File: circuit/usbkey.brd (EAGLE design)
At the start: 78.4 x 68.6 mm, 29 parts, among them IC1 ATmega168P, Q1 16MHz, X2 USB

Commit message: update
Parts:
- removed C5: 1u, resistor:C025-024X044
- removed C6: 0.1u, resistor:C025-024X044
- removed JP1: AVR-ISP-6VERT, avr-7:AVR-ISP-6
- removed JP3: (no value), pinhead:1X09
- removed LED, OUTPUT, SPEAKER: (no value), pinhead:1X02
- removed R5: VARISTOR, varistor:R-5
- removed R9: 1k, resistor:0204/7
- added D3, D4: 5V, diode:DO35Z10
- added P1: SPEAKER, pinhead:1X02
- added P2: LED, pinhead:1X02
- added P3: OUTPUT, pinhead:1X02
- added PISP: AVR-ISP-6VERT, avr-7:AVR-ISP-6
- C1, C2: value 0.1u -> 22p; device resistor:C025-024X044 -> c-j:50-0302-2.54
- C3: device resistor:C025-024X044 -> c-j:50-0302-2.54
- C4: value 1u -> 0.1u; device resistor:C025-024X044 -> c-j:50-0302-2.54
- LED1: value (none) -> MONITOR
- R1, R2: value 168 -> 68; device resistor:0204V -> r-j:1/4W-7.62H
- R3: device resistor:0204/7 -> r-j:1/4W-2.54V
- R4: value VARISTOR -> 1.5k; device varistor:R-5 -> r-j:1/4W-2.54V
- R6: device resistor:0204V -> r-j:1/4W-2.54V
- R7: device resistor:0204V -> r-j:1/4W-7.62H
- R8: device resistor:0204/7 -> r-j:1/4W-7.62H
- moved C4 112.3 mm to (-6.35, -14.0), turned to 0 degrees
- moved R4 63.1 mm to (-7.62, -20.3), turned to 0 degrees
- moved OK1 30.6 mm to (54.6, 8.89)
- moved R7 20.5 mm to (49.5, 5.08)
- moved D2 17.0 mm to (12.7, 35.6)
- moved R1 17.0 mm to (29.2, 38.1)
- moved R2 17.0 mm to (29.2, 40.6)
- moved D1 17.0 mm to (15.2, 33.0)
- moved R8 16.3 mm to (50.8, 49.5)
- moved X2 15.9 mm to (5.08, 36.8)
- moved R3 15.7 mm to (17.8, 38.1)
- moved Q1 14.8 mm to (30.5, 25.4)
- moved IC1 14.8 mm to (39.4, 31.8)
- moved C1 14.8 mm to (24.1, 22.9)
- moved C2 14.8 mm to (24.1, 27.9)
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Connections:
- removed net AVCC: IC1.20
- removed net N$20: C4.1, JP3.2
- removed net N$21: C5.1, JP3.4
- removed net N$22: C5.2, JP3.3
- removed net N$23: IC1.27, JP3.7, R8.1
- removed net N$24: IC1.28, JP3.8, R9.1
- net GND: now also C1.PAD2, C2.PAD2, C3.PAD1, C4.PAD1, D3.A, D4.A, P1.2, PISP.6; no longer C1.2, C2.2, C3.1, C6.2, JP1.6, JP3.6, R4.2, R5.2, SPEAKER.2
- net N$1: now also C1.PAD1; no longer C1.1
- net N$10: now also PISP.4; no longer JP1.4
- net N$11: now also PISP.3; no longer JP1.3
- net N$12: now also PISP.1; no longer JP1.1
- net N$13: now also P2.1, R6.PAD1; no longer LED.1, R6.1
- net N$14: now also P1.1, R7.PAD1; no longer R7.1, SPEAKER.1
- net N$15: now also R7.PAD2; no longer R7.2
- net N$16: now also R6.PAD2; no longer R6.2
- net N$17: now also P2.2; no longer LED.2
- net N$18: now also P3.1; no longer OUTPUT.1
- net N$19: now also P3.2; no longer OUTPUT.2
- net N$2: now also C2.PAD1; no longer C2.1
- net N$3: now also R1.PAD2; no longer R1.2
- net N$4: now also R2.PAD1; no longer R2.1
- net N$5: now also R2.PAD2; no longer R2.2
- net N$6: now also R1.PAD1, R3.PAD1; no longer R1.1, R3.1
- net N$7: now also D3.C; no longer R4.1
- net N$8: now also D4.C; no longer R5.1
- net N$9: now also C4.PAD2, PISP.5, R4.PAD1; no longer JP1.5
- net VCC: now also C3.PAD2, IC1.20, PISP.2, R3.PAD2, R4.PAD2; no longer C3.2, C4.2, C6.1, JP1.2, JP3.5, JP3.9, R3.2, R8.2, R9.2
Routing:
- net VCC: track 134.3 -> 74.0 mm, vias 0 -> 2
- net N$9: track 12.7 -> 61.0 mm, vias 0 -> 2
- net GND: track 218.4 -> 183.1 mm
- net N$24: track 30.5 -> 0.00 mm, vias 2 -> 0
- net N$10: track 64.9 -> 35.6 mm, vias 0 -> 2
- net N$12: track 40.6 -> 12.7 mm
- net N$23: track 27.9 -> 0.00 mm
- net N$11: track 40.6 -> 17.8 mm, vias 0 -> 2
- net N$15: track 2.54 -> 12.7 mm
- net N$22: track 7.62 -> 0.00 mm
- net N$4: track 22.8 -> 19.0 mm
- net N$6: track 19.8 -> 16.0 mm
- net N$8: track 44.9 -> 48.5 mm
- net N$17: track 5.08 -> 2.54 mm
- net N$21: track 2.54 -> 0.00 mm
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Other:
- board size 78.4 x 68.6 mm -> 69 x 95 mm

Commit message: update
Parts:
- removed R8: 1k, r-j:1/4W-7.62H
- added C5, C6: 100p, c-j:50-0302-2.54
- added JP1: (no value), pinhead:1X03
- added JP2: (no value), pinhead:1X06
- moved X1 90.9 mm to (82.5, 48.3)
- moved R4 83.2 mm to (35.6, 50.8), turned to 90 degrees
- moved C4 72.6 mm to (33.0, 47.0), turned to 90 degrees
- moved D4 17.0 mm to (15.2, 17.8)
- moved C3 8.98 mm to (33.0, 31.8), turned to 90 degrees
- moved D3 8.03 mm to (15.2, 20.3)
- moved C1 2.54 mm to (21.6, 22.9)
- moved C2 2.54 mm to (21.6, 27.9)
- moved Q1 2.54 mm to (27.9, 25.4)
- moved R1 2.54 mm to (26.7, 38.1)
- moved R2 2.54 mm to (26.7, 40.6)
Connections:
- new net N$20: IC1.23, JP2.1
- new net N$21: IC1.24, JP2.2
- new net N$22: IC1.25, JP2.3
- new net N$23: IC1.26, JP2.4
- new net N$24: IC1.27, JP2.5
- new net N$25: IC1.28, JP2.6
- net GND: now also C5.PAD2, C6.PAD2, JP1.1; no longer X1.1
- net N$3: now also C5.PAD1
- net N$5: now also C6.PAD1
- net N$7: now also JP1.3; no longer X1.3
- net N$8: now also JP1.2; no longer X1.2
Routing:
- net N$9: track 61.0 -> 5.08 mm, vias 2 -> 0
- net VCC: track 74.0 -> 122.3 mm, vias 2 -> 3
- net N$8: track 48.5 -> 20.3 mm
- net N$7: track 33.3 -> 22.9 mm, vias 0 -> 1
- net GND: track 183.1 -> 175.1 mm
- net N$25: track 0.00 -> 5.08 mm
- net N$24: track 0.00 -> 5.08 mm
- net N$23: track 0.00 -> 5.08 mm
- net N$22: track 0.00 -> 5.08 mm
- net N$21: track 0.00 -> 5.08 mm
- net N$20: track 0.00 -> 5.08 mm
- net N$5: track 2.54 -> 5.08 mm
- net N$3: track 2.54 -> 5.08 mm
- net N$6: track 16.0 -> 13.5 mm
- net N$4: track 19.0 -> 16.5 mm
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
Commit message: update
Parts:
- added C7: 0.1u, c-j:50-0302-2.54
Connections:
- net GND: now also C7.PAD1
- net VCC: now also C7.PAD2
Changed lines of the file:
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@@
 <element name="JP1" library="pinhead" package="1X03" value="" x="20.32" y="12.7"/>
 <element name="JP2" library="pinhead" package="1X06" value="" x="48.26" y="41.91" rot="R90"/>
+<element name="C7" library="c-j" package="50-0302-2.54" value="0.1u" x="-2.54" y="-13.97"/>
 </elements>
 <signals>
@@
 <wire x1="53.34" y1="7.62" x2="50.8" y2="7.62" width="0.8128" layer="16"/>
 <wire x1="50.8" y1="7.62" x2="50.8" y2="2.54" width="0.8128" layer="16"/>
+<contactref element="C7" pad="PAD1"/>
+<wire x1="-3.81" y1="-13.97" x2="10.16" y2="12.7" width="0" layer="19" extent="16-16"/>
 </signal>
 <signal name="N$2">
@@
 <via x="30.48" y="33.02" extent="1-16" drill="0.6" shape="square"/>
 <wire x1="30.48" y1="33.02" x2="33.02" y2="33.02" width="0.8128" layer="16"/>
+<contactref element="C7" pad="PAD2"/>
+<wire x1="-1.27" y1="-13.97" x2="9.79" y2="35.58" width="0" layer="19" extent="1-1"/>
 </signal>
 <signal name="N$4">
@@
 </signal>
 <signal name="N$9">
-<contactref element="PISP" pad="5"/>
 <contactref element="IC1" pad="1"/>
 <contactref element="C4" pad="PAD2"/>
@@
 <wire x1="35.56" y1="48.26" x2="33.02" y2="48.26" width="0.8128" layer="16"/>
 <wire x1="35.56" y1="48.26" x2="35.56" y2="50.8" width="0.8128" layer="16"/>
+<contactref element="PISP" pad="5"/>
 <wire x1="55.88" y1="17.78" x2="35.56" y2="48.26" width="0" layer="19" extent="1-1"/>
 </signal>

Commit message: update
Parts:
- R3: device r-j:1/4W-2.54V -> r-j:1/4W-7.62H
- moved C7 89.3 mm to (41.9, 63.5)
- moved P1 75.2 mm to (67.3, 78.7), turned to 0 degrees
- moved P3 69.9 mm to (62.2, 78.7), turned to 0 degrees
- moved R7 64.4 mm to (66.0, 67.3), turned to 270 degrees
- moved OK1 64.0 mm to (62.2, 72.4), turned to 0 degrees
- moved JP1 57.1 mm to (68.6, 43.2), turned to 90 degrees
- moved P2 55.8 mm to (59.7, 66.0), turned to 0 degrees
- moved PISP 55.0 mm to (50.8, 74.9), turned to 0 degrees
- moved D4 50.0 mm to (61.0, 38.1), turned to 270 degrees
- moved R6 48.5 mm to (53.3, 66.0), turned to 270 degrees
- moved D3 46.7 mm to (58.4, 38.1), turned to 270 degrees
- moved JP2 30.7 mm to (29.2, 66.0), turned to 180 degrees
- moved C1 30.1 mm to (48.3, 36.8), turned to 270 degrees
- moved IC1 25.4 mm to (39.4, 57.1), turned to 0 degrees
- moved Q1 25.1 mm to (45.7, 43.2), turned to 180 degrees
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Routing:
- net GND: track 175.1 -> 225.6 mm
- net N$3: track 5.08 -> 22.9 mm, vias 0 -> 2
- net N$5: track 5.08 -> 15.2 mm, vias 0 -> 2
- net N$7: track 22.9 -> 27.9 mm
- net N$8: track 20.3 -> 25.4 mm
- net N$6: track 13.5 -> 10.6 mm
- net N$2: track 12.7 -> 15.2 mm
- net N$1: track 13.8 -> 15.8 mm
- net N$4: track 16.5 -> 15.1 mm
- net VCC: vias 3 -> 0
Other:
- board size 69 x 95 mm -> 95 x 69 mm

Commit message: F_CPU 18MHz
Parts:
- Q1: value 16MHz -> 18MHz
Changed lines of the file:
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@@
 <attribute name="OC_FARNELL" value="unknown" x="71.12" y="5.08" size="1.778" layer="27" display="off"/>
 </element>
-<element name="Q1" library="special" package="QS" value="16MHz" x="45.72" y="43.18" rot="R180"/>
+<element name="Q1" library="special" package="QS" value="18MHz" x="45.72" y="43.18" rot="R180"/>
 <element name="C1" library="c-j" package="50-0302-2.54" value="22p" x="48.26" y="36.83" smashed="yes" rot="R270">
 <attribute name="NAME" x="46.355" y="34.798" size="1.27" layer="25" ratio="10" rot="R270"/>

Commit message: update
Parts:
- moved X1 12.0 mm to (88.9, 38.1), turned to 270 degrees
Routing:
- net GND: track 225.6 -> 208.3 mm

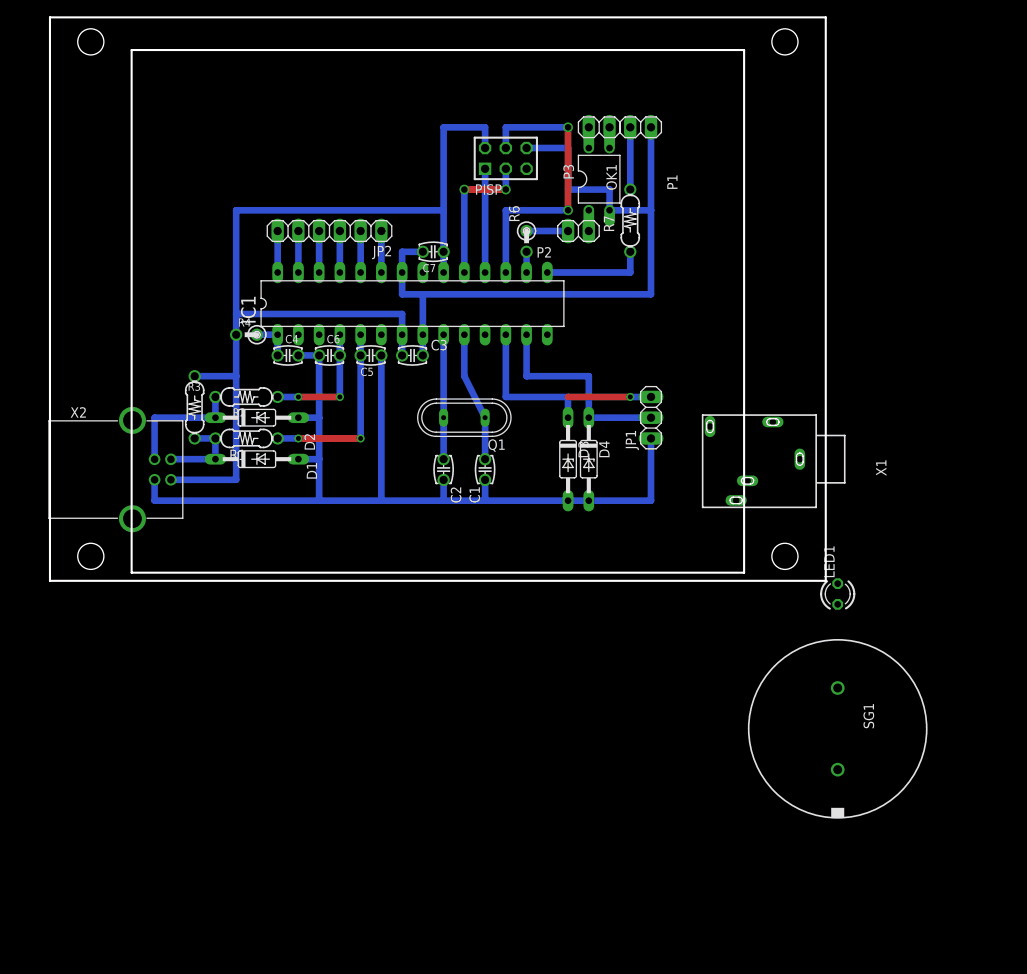
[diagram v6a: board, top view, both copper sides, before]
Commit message: reset の 0.1u は ISP ができなくなる
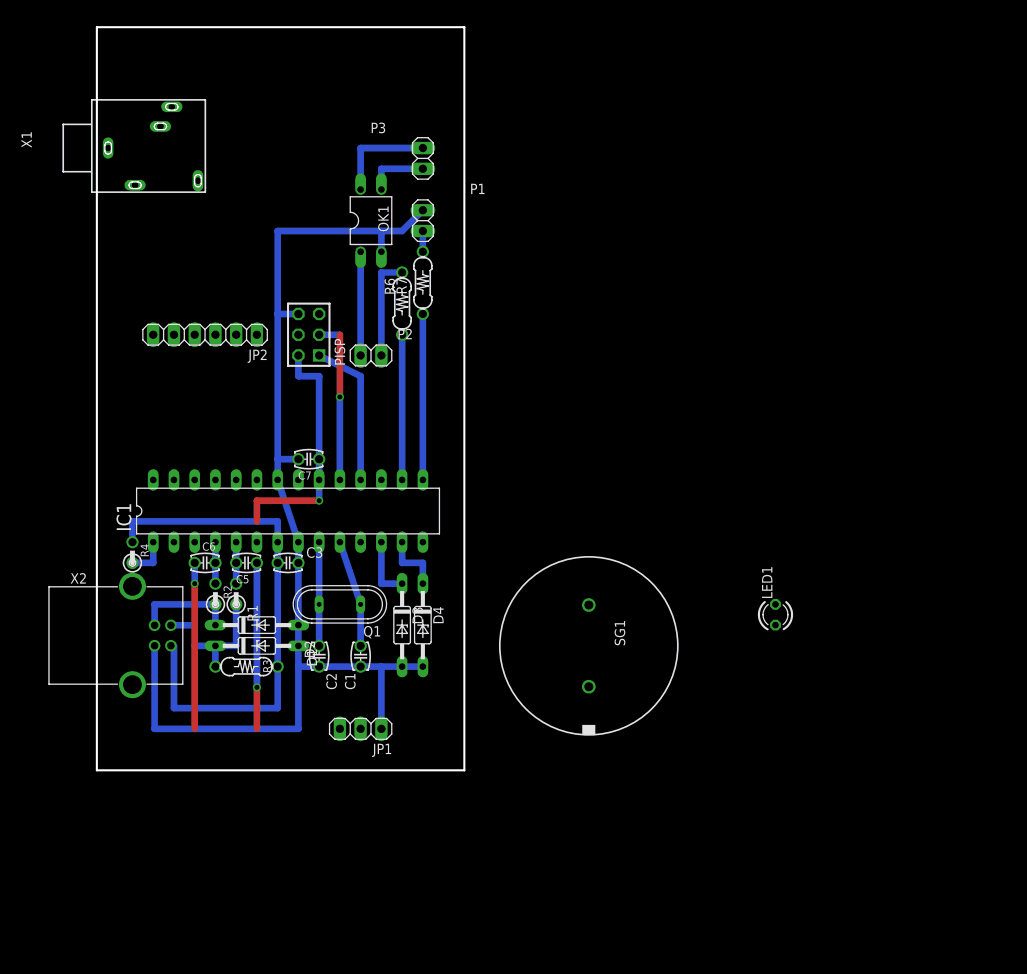
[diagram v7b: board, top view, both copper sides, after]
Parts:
- removed C4: 0.1u, c-j:50-0302-2.54
- R1, R2: device r-j:1/4W-7.62H -> r-j:1/4W-2.54V
- R6: device r-j:1/4W-2.54V -> r-j:1/4W-7.62H
- moved X1 96.7 mm to (0.00, 76.2), turned to 90 degrees
- moved JP1 52.1 mm to (33.0, 5.08), turned to 180 degrees
- moved R3 32.4 mm to (19.1, 12.7), turned to 0 degrees
- moved PISP 32.4 mm to (26.7, 53.3), turned to 90 degrees
- moved SG1 32.1 mm to (61.0, 15.2)
- moved R4 31.8 mm to (5.08, 25.4), turned to 90 degrees
- moved P2 29.6 mm to (34.3, 50.8), turned to 180 degrees
- moved C6 29.6 mm to (14.0, 25.4)
- moved C3 29.6 mm to (24.1, 25.4)
- moved C5 29.6 mm to (19.1, 25.4)
- moved C7 29.6 mm to (26.7, 38.1)
- moved IC1 29.6 mm to (24.1, 31.8)
- moved P1 29.0 mm to (40.6, 67.3), turned to 90 degrees
- moved D3 28.7 mm to (38.1, 17.8)
- moved D4 28.7 mm to (40.6, 17.8)
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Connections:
- net N$18 renamed OUT+
- net N$19 renamed OUT-
- net GND: no longer C4.PAD1
- net N$9: no longer C4.PAD2
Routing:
- net N$10: track 35.6 -> 0.00 mm, vias 2 -> 0
- net GND: track 208.3 -> 179.1 mm, vias 0 -> 2
- net VCC: track 122.3 -> 94.4 mm, vias 0 -> 1
- net N$7: track 27.9 -> 7.62 mm, vias 1 -> 0
- net N$3: track 22.9 -> 5.08 mm, vias 2 -> 0
- net N$8: track 25.4 -> 7.62 mm
- net N$16: track 2.54 -> 17.8 mm
- net N$17: track 2.54 -> 12.7 mm
- net OUT+: track 2.54 -> 12.7 mm
- net N$5: track 15.2 -> 5.08 mm, vias 2 -> 0
- net N$13: track 5.08 -> 12.7 mm
- net N$15: track 12.7 -> 20.3 mm
- net N$6: track 10.6 -> 18.1 mm
- net N$12: track 12.7 -> 18.4 mm
- net N$25: track 5.08 -> 0.00 mm
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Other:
- board size 95 x 69 mm -> 45 x 91 mm

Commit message: update
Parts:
- removed JP2: (no value), pinhead:1X06
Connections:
- removed net N$20: IC1.23, JP2.1
- removed net N$21: IC1.24, JP2.2
- removed net N$22: IC1.25, JP2.3
- removed net N$23: IC1.26, JP2.4
- removed net N$24: IC1.27, JP2.5
- removed net N$25: IC1.28, JP2.6
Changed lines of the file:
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@@
 <element name="C6" library="c-j" package="50-0302-2.54" value="100p" x="13.97" y="25.4" rot="R180"/>
 <element name="JP1" library="pinhead" package="1X03" value="" x="33.02" y="5.08" rot="R180"/>
-<element name="JP2" library="pinhead" package="1X06" value="" x="13.97" y="53.34" rot="R180"/>
 <element name="C7" library="c-j" package="50-0302-2.54" value="0.1u" x="26.67" y="38.1"/>
 </elements>
@@
 <wire x1="33.02" y1="50.8" x2="33.02" y2="63.5" width="0.8128" layer="16"/>
 </signal>
-<signal name="N$20">
-<contactref element="JP2" pad="1"/>
-<contactref element="IC1" pad="23"/>
-<wire x1="20.32" y1="35.56" x2="20.32" y2="53.34" width="0" layer="19" extent="1-1"/>
-</signal>
-<signal name="N$21">
-<contactref element="JP2" pad="2"/>
-<contactref element="IC1" pad="24"/>
-<wire x1="17.78" y1="35.56" x2="17.78" y2="53.34" width="0" layer="19" extent="1-1"/>
-</signal>
-<signal name="N$22">
-<contactref element="JP2" pad="3"/>
-<contactref element="IC1" pad="25"/>
-<wire x1="15.24" y1="35.56" x2="15.24" y2="53.34" width="0" layer="19" extent="1-1"/>
-</signal>
-<signal name="N$23">
-<contactref element="JP2" pad="4"/>
-<contactref element="IC1" pad="26"/>
-<wire x1="12.7" y1="35.56" x2="12.7" y2="53.34" width="0" layer="19" extent="1-1"/>
-</signal>
-<signal name="N$24">
-<contactref element="JP2" pad="5"/>
-<contactref element="IC1" pad="27"/>
-<wire x1="10.16" y1="35.56" x2="10.16" y2="53.34" width="0" layer="19" extent="1-1"/>
-</signal>
-<signal name="N$25">
-<contactref element="JP2" pad="6"/>
-<contactref element="IC1" pad="28"/>
-<wire x1="7.62" y1="35.56" x2="7.62" y2="53.34" width="0" layer="19" extent="1-1"/>
-</signal>
 <signal name="GND1">
